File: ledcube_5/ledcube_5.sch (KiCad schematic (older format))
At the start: 65 parts, among them J1 Conn_01x05_MountingPin, J2 Conn_01x01, J3 Conn_01x01, J4 Conn_01x01, J5 Conn_01x01, J6 Conn_01x01, Q1 PN2222A, Q2 PN2222A, Q3 PN2222A, Q4 PN2222A, Q5 PN2222A, U1 74HC595, U2 74HC595, U3 74HC595, U4 74HC595

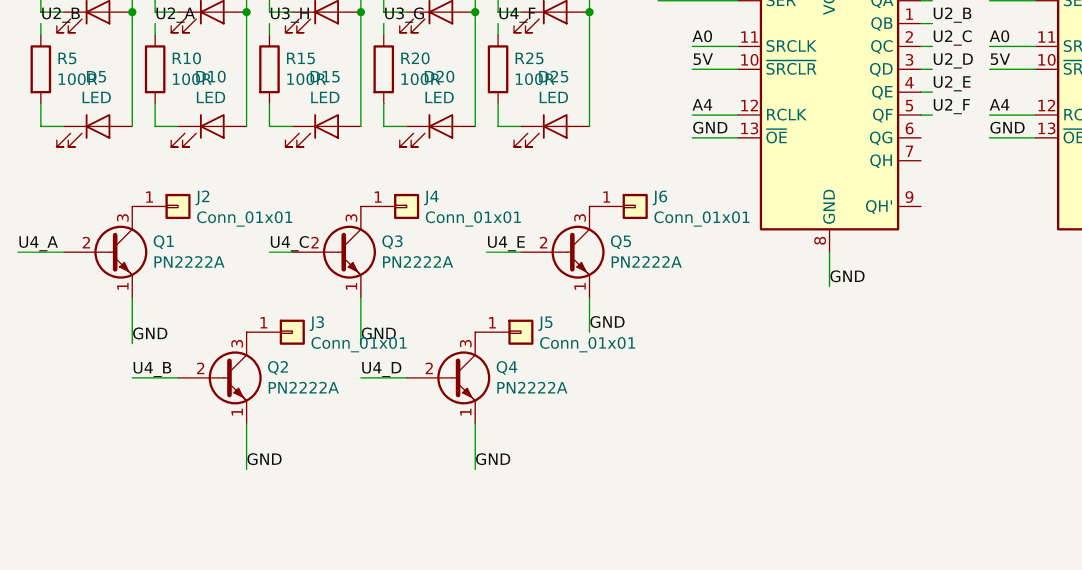
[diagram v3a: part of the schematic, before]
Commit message: fix missing R for transistors
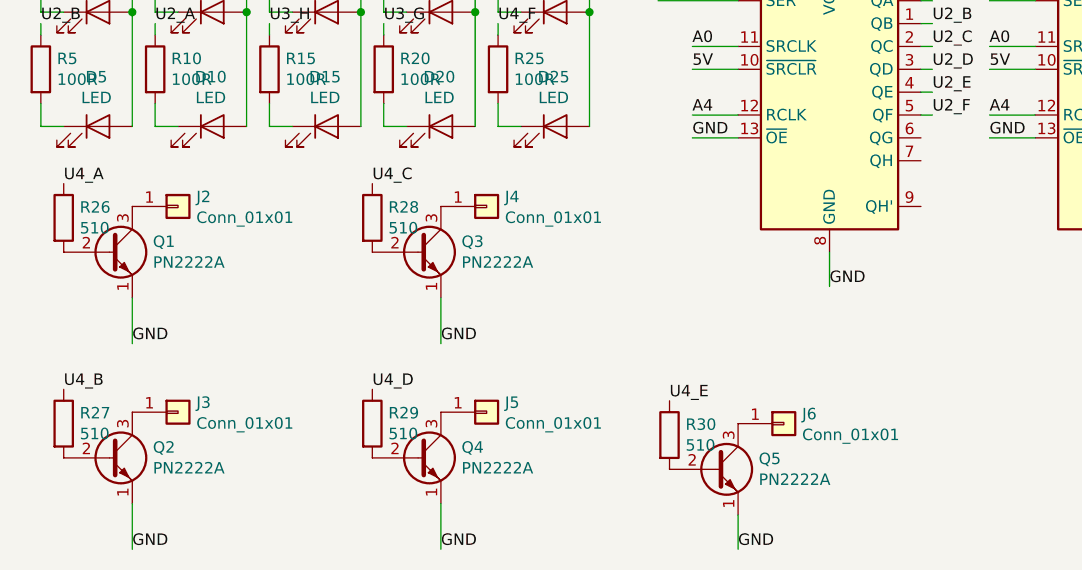
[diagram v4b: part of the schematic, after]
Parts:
- added R26, R27, R28, R29, R30: 510, Resistor_THT:R_Axial_DIN0207_L6.3mm_D2.5mm_P10.16mm_Horizontal, symbol Device:R
- J1: footprint Connector_PinHeader_2.00mm:PinHeader_1x05_P2.00mm_Vertical -> Connector_PinHeader_2.54mm:PinHeader_1x05_P2.54mm_Vertical
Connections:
- net U4_A: now also R26.1; no longer Q1.2 (B)
- net U4_B: now also R27.1; no longer Q2.2 (B)
- net U4_C: now also R28.1; no longer Q3.2 (B)
- net U4_D: now also R29.1; no longer Q4.2 (B)
- net U4_E: now also R30.1; no longer Q5.2 (B)
- new net: Q3.2 (B), R28.2
- new net: Q2.2 (B), R27.2
- new net: Q1.2 (B), R26.2
- new net: Q4.2 (B), R29.2
- new net: Q5.2 (B), R30.2
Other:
- moved on the sheet: J3, J4, J5, J6, Q2, Q3, Q4, Q5
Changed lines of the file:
@@
 L Transistor_BJT:PN2222A Q3
 U 1 1 610B975C
-P 2300 3800
-F 0 "Q3" H 2490 3846 50  0000 L CNN
-F 1 "PN2222A" H 2490 3755 50  0000 L CNN
-F 2 "Package_TO_SOT_THT:TO-92_Inline" H 2500 3725 50  0001 L CIN
-F 3 "https://www.onsemi.com/pub/Collateral/PN2222-D.PDF" H 2300 3800 50  0001 L CNN
-	1    2300 3800
+P 2650 3800
+F 0 "Q3" H 2840 3846 50  0000 L CNN
+F 1 "PN2222A" H 2840 3755 50  0000 L CNN
+F 2 "Package_TO_SOT_THT:TO-92_Inline" H 2850 3725 50  0001 L CIN
+F 3 "https://www.onsemi.com/pub/Collateral/PN2222-D.PDF" H 2650 3800 50  0001 L CNN
+	1    2650 3800
 	1    0    0    -1
 $EndComp
@@
 L Transistor_BJT:PN2222A Q2
 U 1 1 610BA815
-P 1800 4350
-F 0 "Q2" H 1990 4396 50  0000 L CNN
-F 1 "PN2222A" H 1990 4305 50  0000 L CNN
-F 2 "Package_TO_SOT_THT:TO-92_Inline" H 2000 4275 50  0001 L CIN
-F 3 "https://www.onsemi.com/pub/Collateral/PN2222-D.PDF" H 1800 4350 50  0001 L CNN
-	1    1800 4350
+P 1300 4700
+F 0 "Q2" H 1490 4746 50  0000 L CNN
+F 1 "PN2222A" H 1490 4655 50  0000 L CNN
+F 2 "Package_TO_SOT_THT:TO-92_Inline" H 1500 4625 50  0001 L CIN
+F 3 "https://www.onsemi.com/pub/Collateral/PN2222-D.PDF" H 1300 4700 50  0001 L CNN
+	1    1300 4700
 	1    0    0    -1
 $EndComp
@@
 L Transistor_BJT:PN2222A Q4
 U 1 1 610E6DE4
-P 2800 4350
-F 0 "Q4" H 2990 4396 50  0000 L CNN
-F 1 "PN2222A" H 2990 4305 50  0000 L CNN
-F 2 "Package_TO_SOT_THT:TO-92_Inline" H 3000 4275 50  0001 L CIN
-F 3 "https://www.onsemi.com/pub/Collateral/PN2222-D.PDF" H 2800 4350 50  0001 L CNN
-	1    2800 4350
+P 2650 4700
+F 0 "Q4" H 2840 4746 50  0000 L CNN
+F 1 "PN2222A" H 2840 4655 50  0000 L CNN
+F 2 "Package_TO_SOT_THT:TO-92_Inline" H 2850 4625 50  0001 L CIN
+F 3 "https://www.onsemi.com/pub/Collateral/PN2222-D.PDF" H 2650 4700 50  0001 L CNN
+	1    2650 4700
 	1    0    0    -1
 $EndComp
@@
 L Transistor_BJT:PN2222A Q5
 U 1 1 610E745F
-P 3300 3800
-F 0 "Q5" H 3490 3846 50  0000 L CNN
-F 1 "PN2222A" H 3490 3755 50  0000 L CNN
-F 2 "Package_TO_SOT_THT:TO-92_Inline" H 3500 3725 50  0001 L CIN
-F 3 "https://www.onsemi.com/pub/Collateral/PN2222-D.PDF" H 3300 3800 50  0001 L CNN
-	1    3300 3800
+P 3950 4750
+F 0 "Q5" H 4140 4796 50  0000 L CNN
+F 1 "PN2222A" H 4140 4705 50  0000 L CNN
+F 2 "Package_TO_SOT_THT:TO-92_Inline" H 4150 4675 50  0001 L CIN
+F 3 "https://www.onsemi.com/pub/Collateral/PN2222-D.PDF" H 3950 4750 50  0001 L CNN
+	1    3950 4750
 	1    0    0    -1
 $EndComp
@@
 Text Label 6200 2800 0    50   ~ 0
 U4_B
-Text Label 1400 4350 0    50   ~ 0
+Text Label 1100 4400 0    50   ~ 0
 U4_B
 Text Label 6200 2700 0    50   ~ 0
 U4_A
-Text Label 900  3800 0    50   ~ 0
+Text Label 1100 3500 0    50   ~ 0
 U4_A
-Wire Wire Line
-	900  3800 1100 3800
-Wire Wire Line
-	1400 4350 1600 4350
 Text Label 6200 2900 0    50   ~ 0
 U4_C
-Text Label 2000 3800 0    50   ~ 0
+Text Label 2450 3500 0    50   ~ 0
 U4_C
-Wire Wire Line
-	2000 3800 2100 3800
 Text Label 6200 3000 0    50   ~ 0
 U4_D
-Text Label 2400 4350 0    50   ~ 0
+Text Label 2450 4400 0    50   ~ 0
 U4_D
-Wire Wire Line
-	2600 4350 2400 4350
 Text Label 6200 3100 0    50   ~ 0
 U4_E
-Text Label 2950 3800 0    50   ~ 0
+Text Label 3750 4450 0    50   ~ 0
 U4_E
-Wire Wire Line
-	2950 3800 3100 3800
 Text Label 6200 3200 0    50   ~ 0
 U4_F
@@
 Text Label 1400 4200 0    50   ~ 0
 GND
-Text Label 1900 4750 0    50   ~ 0
-GND
-Text Label 2400 4200 0    50   ~ 0
-GND
-Text Label 2900 4750 0    50   ~ 0
-GND
-Text Label 3400 4150 0    50   ~ 0
+Text Label 1400 5100 0    50   ~ 0
+GND
+Text Label 2750 4200 0    50   ~ 0
+GND
+Text Label 2750 5100 0    50   ~ 0
+GND
+Text Label 4050 5100 0    50   ~ 0
 GND
 $Comp
@@
 F 0 "J1" H 7738 1964 50  0000 L CNN
 F 1 "Conn_01x05_MountingPin" H 7738 1873 50  0000 L CNN
-F 2 "Connector_PinHeader_2.00mm:PinHeader_1x05_P2.00mm_Vertical" H 7650 2000 50  0001 C CNN
+F 2 "Connector_PinHeader_2.54mm:PinHeader_1x05_P2.54mm_Vertical" H 7650 2000 50  0001 C CNN
 F 3 "~" H 7650 2000 50  0001 C CNN
 	1    7650 2000
@@
 	6200 2200 5750 2200
 Wire Wire Line
-	3400 4000 3400 4150
-Wire Wire Line
-	2900 4750 2900 4550
-Wire Wire Line
-	1900 4750 1900 4550
+	4050 4950 4050 5100
+Wire Wire Line
+	2750 5100 2750 4900
+Wire Wire Line
+	1400 5100 1400 4900
 Wire Wire Line
 	1400 4000 1400 4200
 Wire Wire Line
-	2400 4200 2400 4000
+	2750 4200 2750 4000
 Wire Wire Line
 	4450 2200 3900 2200
@@
 L Connector_Generic:Conn_01x01 J6
 U 1 1 611441A3
-P 3600 3600
-F 0 "J6" H 3680 3642 50  0000 L CNN
-F 1 "Conn_01x01" H 3680 3551 50  0000 L CNN
-F 2 "Connector_Pin:Pin_D1.0mm_L10.0mm" H 3600 3600 50  0001 C CNN
-F 3 "~" H 3600 3600 50  0001 C CNN
-	1    3600 3600
+P 4250 4550
+F 0 "J6" H 4330 4592 50  0000 L CNN
+F 1 "Conn_01x01" H 4330 4501 50  0000 L CNN
+F 2 "Connector_Pin:Pin_D1.0mm_L10.0mm" H 4250 4550 50  0001 C CNN
+F 3 "~" H 4250 4550 50  0001 C CNN
+	1    4250 4550
 	1    0    0    -1
 $EndComp
@@
 L Connector_Generic:Conn_01x01 J5
 U 1 1 61143AA4
-P 3100 4150
-F 0 "J5" H 3180 4192 50  0000 L CNN
-F 1 "Conn_01x01" H 3180 4101 50  0000 L CNN
-F 2 "Connector_Pin:Pin_D1.0mm_L10.0mm" H 3100 4150 50  0001 C CNN
-F 3 "~" H 3100 4150 50  0001 C CNN
-	1    3100 4150
+P 2950 4500
+F 0 "J5" H 3030 4542 50  0000 L CNN
+F 1 "Conn_01x01" H 3030 4451 50  0000 L CNN
+F 2 "Connector_Pin:Pin_D1.0mm_L10.0mm" H 2950 4500 50  0001 C CNN
+F 3 "~" H 2950 4500 50  0001 C CNN
+	1    2950 4500
 	1    0    0    -1
 $EndComp
@@
 L Connector_Generic:Conn_01x01 J3
 U 1 1 61142E71
-P 2100 4150
-F 0 "J3" H 2180 4192 50  0000 L CNN
-F 1 "Conn_01x01" H 2180 4101 50  0000 L CNN
-F 2 "Connector_Pin:Pin_D1.0mm_L10.0mm" H 2100 4150 50  0001 C CNN
-F 3 "~" H 2100 4150 50  0001 C CNN
-	1    2100 4150
+P 1600 4500
+F 0 "J3" H 1680 4542 50  0000 L CNN
+F 1 "Conn_01x01" H 1680 4451 50  0000 L CNN
+F 2 "Connector_Pin:Pin_D1.0mm_L10.0mm" H 1600 4500 50  0001 C CNN
+F 3 "~" H 1600 4500 50  0001 C CNN
+	1    1600 4500
 	1    0    0    -1
 $EndComp
@@
 L Connector_Generic:Conn_01x01 J4
 U 1 1 61143492
-P 2600 3600
-F 0 "J4" H 2680 3642 50  0000 L CNN
-F 1 "Conn_01x01" H 2680 3551 50  0000 L CNN
-F 2 "Connector_Pin:Pin_D1.0mm_L10.0mm" H 2600 3600 50  0001 C CNN
-F 3 "~" H 2600 3600 50  0001 C CNN
-	1    2600 3600
-	1    0    0    -1
-$EndComp
+P 2950 3600
+F 0 "J4" H 3030 3642 50  0000 L CNN
+F 1 "Conn_01x01" H 3030 3551 50  0000 L CNN
+F 2 "Connector_Pin:Pin_D1.0mm_L10.0mm" H 2950 3600 50  0001 C CNN
+F 3 "~" H 2950 3600 50  0001 C CNN
+	1    2950 3600
+	1    0    0    -1
+$EndComp
+$Comp
+L Device:R R26
+U 1 1 6115B9FB
+P 1100 3650
+F 0 "R26" H 1170 3696 50  0000 L CNN
+F 1 "510" H 1170 3605 50  0000 L CNN
+F 2 "Resistor_THT:R_Axial_DIN0207_L6.3mm_D2.5mm_P10.16mm_Horizontal" V 1030 3650 50  0001 C CNN
+F 3 "~" H 1100 3650 50  0001 C CNN
+	1    1100 3650
+	1    0    0    -1
+$EndComp
+$Comp
+L Device:R R28
+U 1 1 6117195B
+P 2450 3650
+F 0 "R28" H 2520 3696 50  0000 L CNN
+F 1 "510" H 2520 3605 50  0000 L CNN
+F 2 "Resistor_THT:R_Axial_DIN0207_L6.3mm_D2.5mm_P10.16mm_Horizontal" V 2380 3650 50  0001 C CNN
+F 3 "~" H 2450 3650 50  0001 C CNN
+	1    2450 3650
+	1    0    0    -1
+$EndComp
+$Comp
+L Device:R R27
+U 1 1 61171FE9
+P 1100 4550
+F 0 "R27" H 1170 4596 50  0000 L CNN
+F 1 "510" H 1170 4505 50  0000 L CNN
+F 2 "Resistor_THT:R_Axial_DIN0207_L6.3mm_D2.5mm_P10.16mm_Horizontal" V 1030 4550 50  0001 C CNN
+F 3 "~" H 1100 4550 50  0001 C CNN
+	1    1100 4550
+	1    0    0    -1
+$EndComp
+$Comp
+L Device:R R29
+U 1 1 611727CC
+P 2450 4550
+F 0 "R29" H 2520 4596 50  0000 L CNN
+F 1 "510" H 2520 4505 50  0000 L CNN
+F 2 "Resistor_THT:R_Axial_DIN0207_L6.3mm_D2.5mm_P10.16mm_Horizontal" V 2380 4550 50  0001 C CNN
+F 3 "~" H 2450 4550 50  0001 C CNN
+	1    2450 4550
+	1    0    0    -1
+$EndComp
+$Comp
+L Device:R R30
+U 1 1 61172EF5
+P 3750 4600
+F 0 "R30" H 3820 4646 50  0000 L CNN
+F 1 "510" H 3820 4555 50  0000 L CNN
+F 2 "Resistor_THT:R_Axial_DIN0207_L6.3mm_D2.5mm_P10.16mm_Horizontal" V 3680 4600 50  0001 C CNN
+F 3 "~" H 3750 4600 50  0001 C CNN
+	1    3750 4600
+	1    0    0    -1
+$EndComp

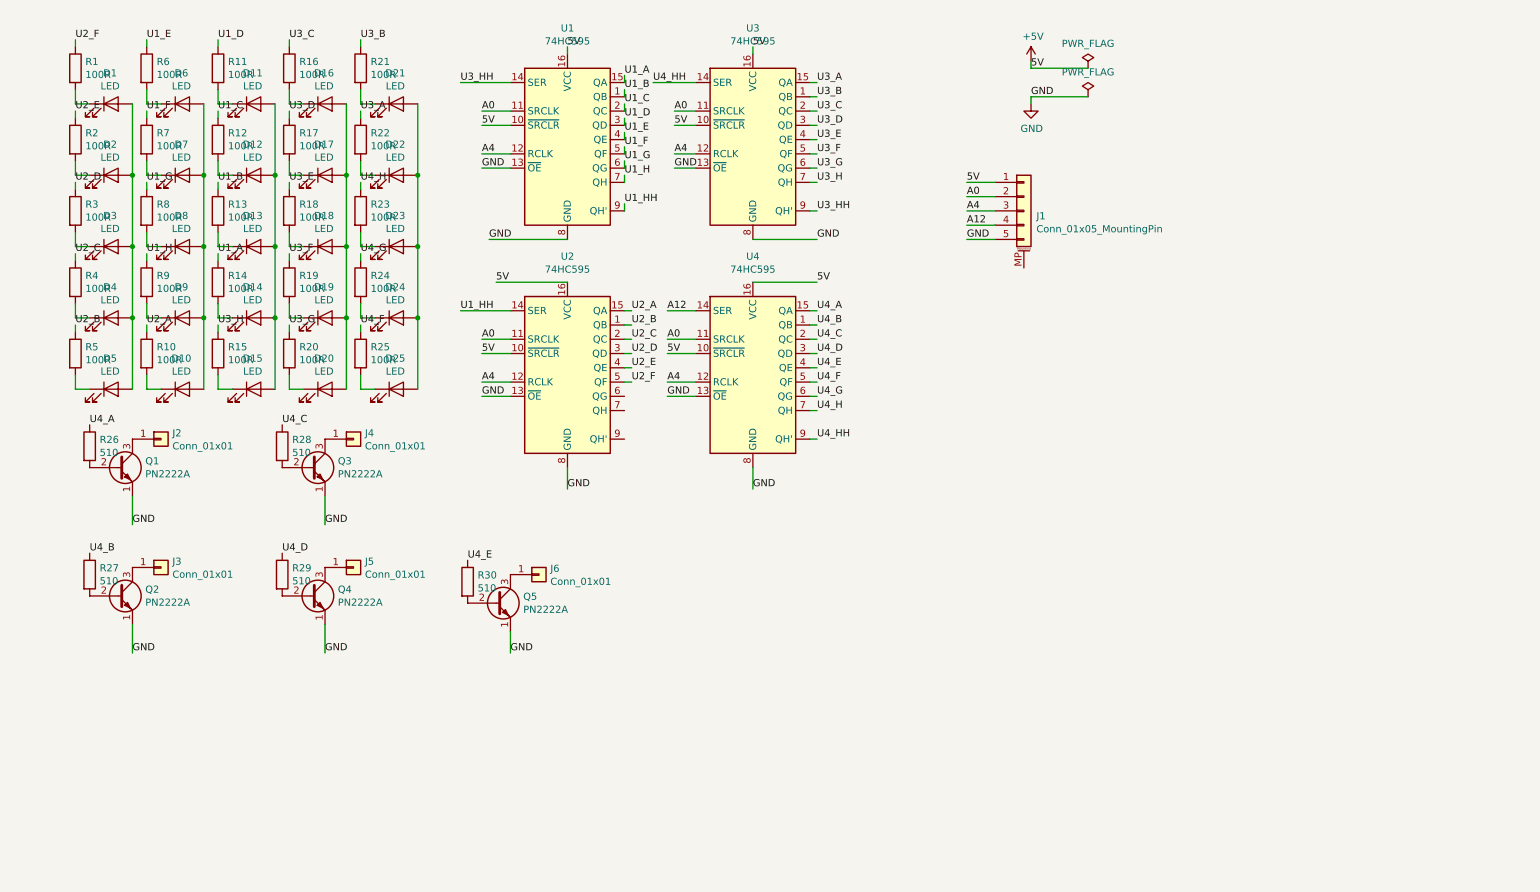
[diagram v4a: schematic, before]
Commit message: ledcube mounting holes and silkscreen
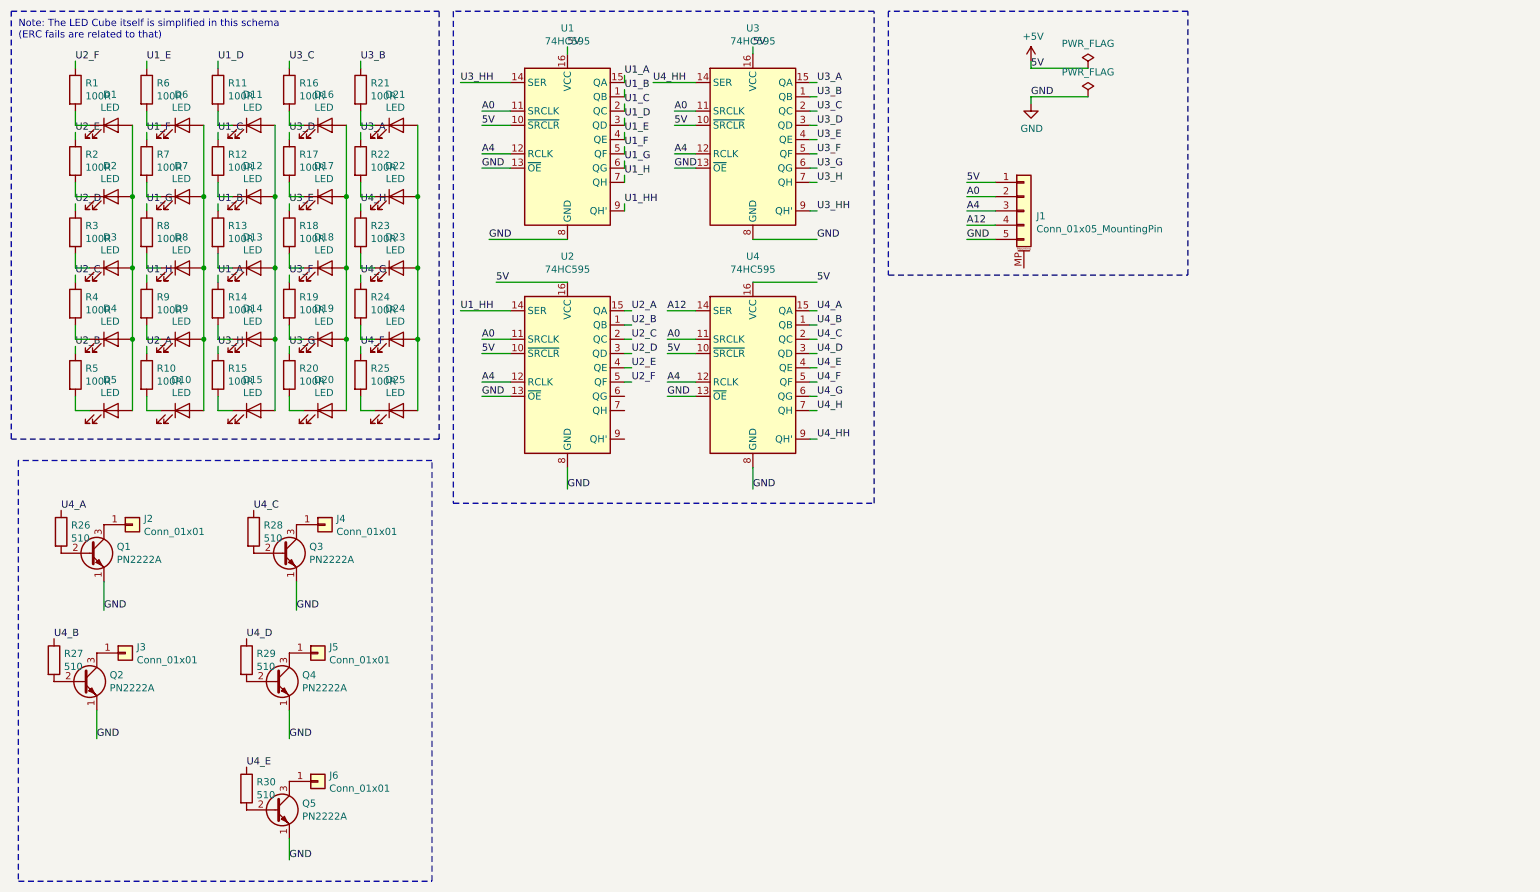
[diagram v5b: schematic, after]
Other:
- note added: "Note: The LED Cube itself is simplified in this schema\n(ERC fails are related to that)"
- moved on the sheet: D1, D10, D11, D12, D13, D14, D15, D16, D17, D18, D19, D2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
